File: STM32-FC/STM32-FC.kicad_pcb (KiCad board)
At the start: 4 copper layers, 39 x 48.5 mm, 114 parts, among them J1 GH 1.25mm 6P, J10 GH 1.25mm 6P, J11 GH 1.25mm 6P, J12 GH 1.25mm 6P, J13 GH 1.25mm 4P, J14 GH 1.25mm 4P, J15 GH 1.25mm 4P, J2 USB_C_USB2.0_14P, J3 GH 1.25mm 6P, J4 TF-06A, J5 JST ZH 1.5mm 2P, J6 PWM_Conn_3x14, J7 ZH 1.5mm 3P, J8 ZH 1.5mm 4P, J9 GH 1.25mm 10P, Q1 S9013, Q2 S9013, SW2 SW_DIP_x03, U1 STM32F407VETx, U10 ATA6561-GBQW, U11 ATA6561-GBQW, U2 USBLC6-2SC6, U3 AMS1117-3.3, U4 AMS1117-3.3, U5 W25X40CLUXIG, U6 BMI323, U7 ICM-42688-P, U8 LIS2MDLTR, U9 LPS22HH, Y1 16MHz

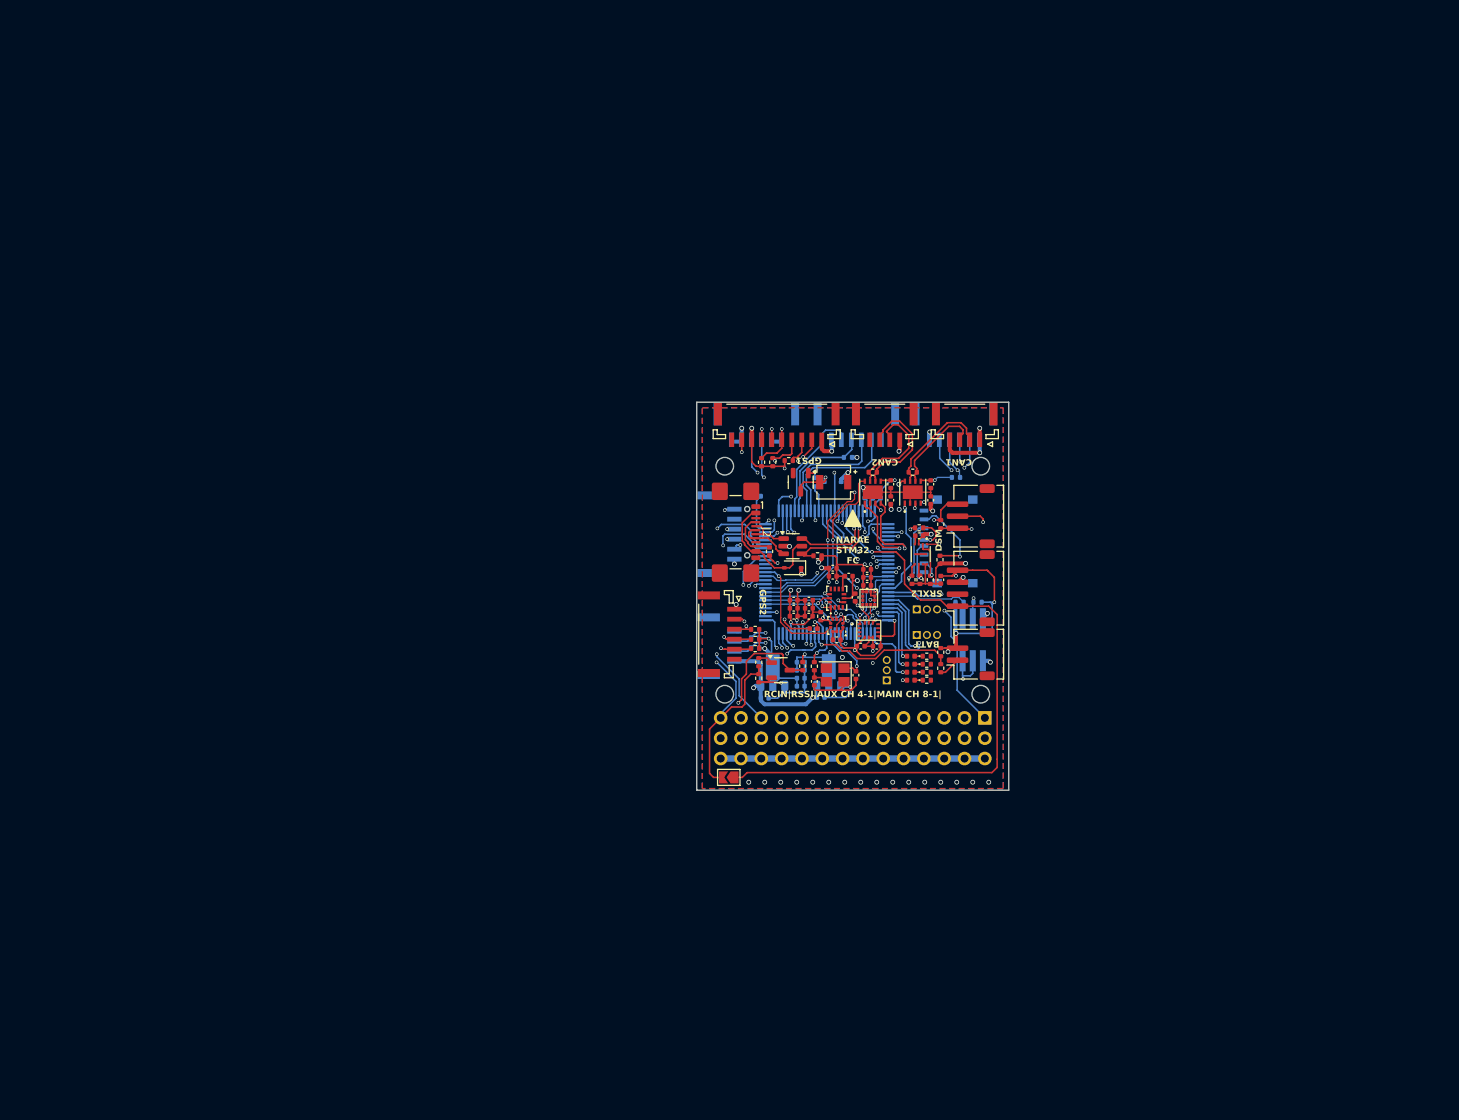
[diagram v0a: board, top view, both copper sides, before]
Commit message: update : BJT to MOSFET
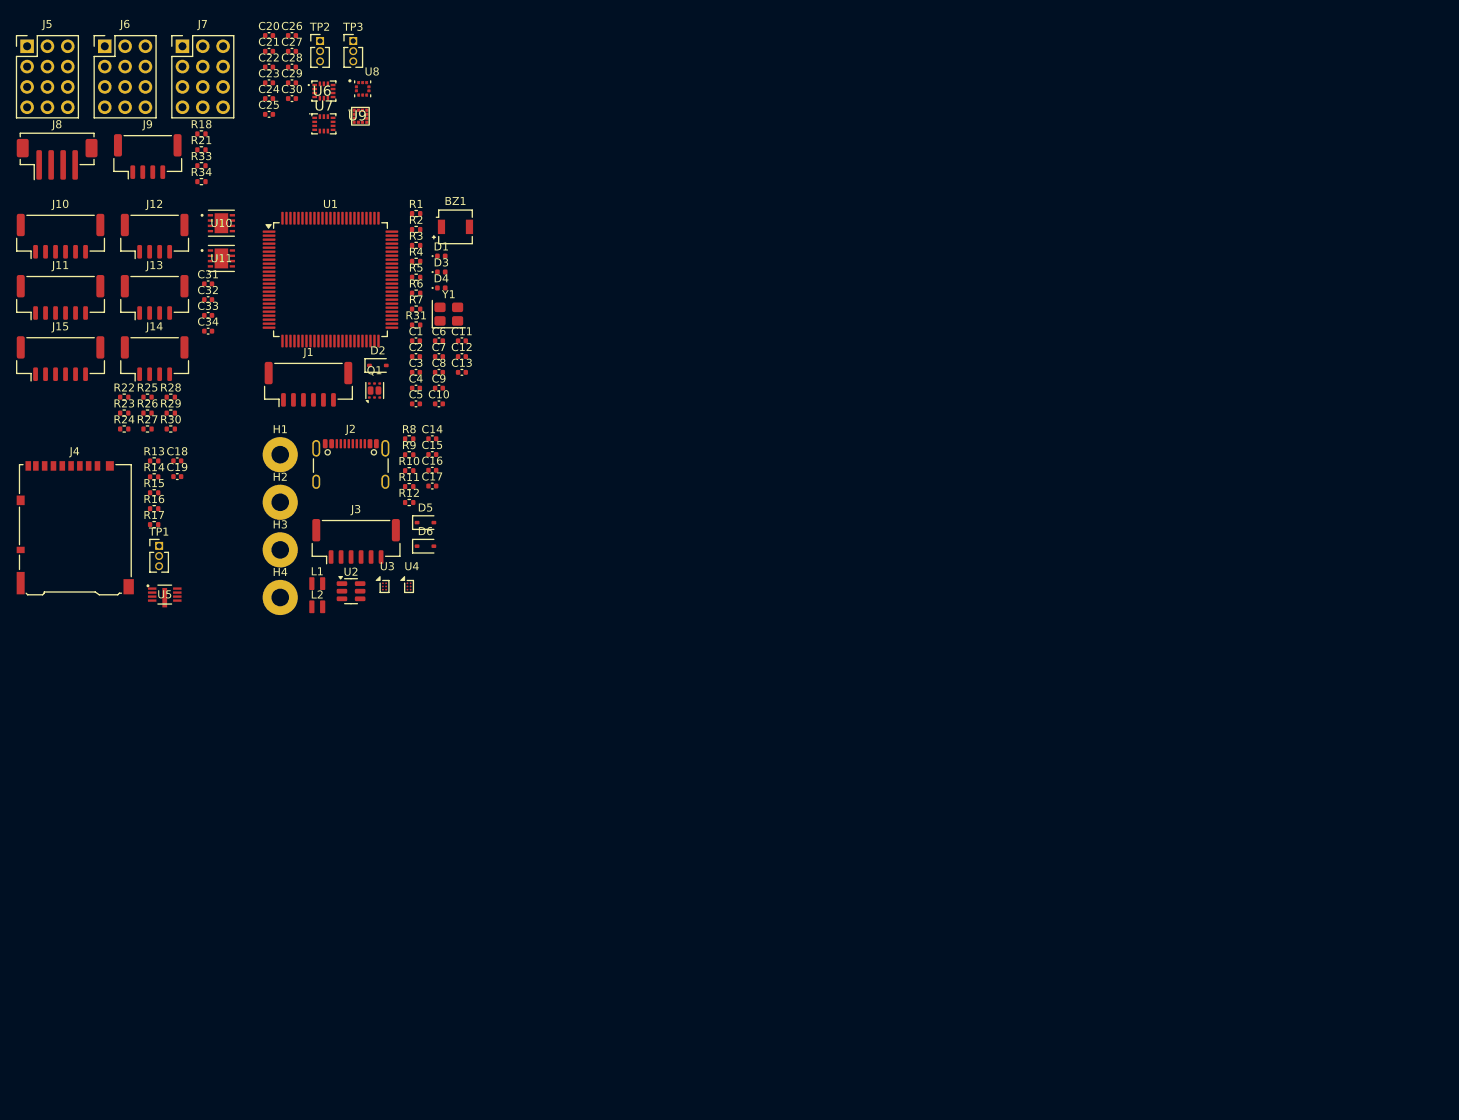
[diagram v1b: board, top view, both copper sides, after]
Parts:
- removed C35: 100nF, Capacitor_SMD:C_0402_1005Metric
- removed JP1: SolderJumper_2_Open, Jumper:SolderJumper-2_P1.3mm_Open_TrianglePad1.0x1.5mm
- removed Q2: S9013, Package_TO_SOT_SMD:SOT-23-3
- removed R19, R20, R32: 10k, Resistor_SMD:R_0402_1005Metric
- removed SW2: SW_DIP_x03, Button_Switch_SMD:SW_DIP_SPSTx03_Slide_KingTek_DSHP03TJ_W5.25mm_P1.27mm_JPin
- added L1: 2.2u, VLS201610ET-2R2M:VLS201610ET-2R2M, F.Cu at (72.1, 92.2)
- added L2: 2.2u, VLS201610ET-2R2M:VLS201610ET-2R2M, F.Cu at (72.1, 95.1)
- C11: value 1uF -> 100nF; moved to F.Cu
- C12: value 100nF -> 1uF; moved to F.Cu
- C13, C18: value 10uF -> 100nF; moved to F.Cu
- C14: value 10uF -> 4.7uF; moved to F.Cu
- C15: value 100nF -> 4.7uF; moved to F.Cu
- C16: value 100nF -> 10uF; moved to F.Cu
- C17, R1, R29, R30, R31, TP1, TP2, TP3, U1: moved to F.Cu
- C20: value 100nF -> 10nF
- C21: value 100nF -> 100pF
- C22: value 100pF -> 100nF
- C23: value 100nF -> 2.2nF
- C24: value 2.2nF -> 100nF
- C25: value 10nF -> 100nF
- C26: value 4.7uF -> 10uF
- C27: value 10uF -> 100nF
- C29: value 100nF -> 220nF
- C30: value 220nF -> 100nF
- C5, C6: value 2.2uF -> 100nF; moved to F.Cu
- C7, C8: value 100nF -> 2.2uF
- D1: value White -> Red
- D2: value Red -> B5819W; footprint LED_SMD:LED_0402_1005Metric -> Diode_SMD:D_SOD-323
- D3: value B5819W -> Yellow; footprint Diode_SMD:D_SOD-323 -> LED_SMD:LED_0402_1005Metric; moved to F.Cu
- D4: value Yellow -> Blue
- D5: value Blue -> B5819W; footprint LED_SMD:LED_0402_1005Metric -> Diode_SMD:D_SOD-323
- H1, H2, H3, H4: footprint Hole:MountingHole_2.2mm_M2 -> MountingHole:MountingHole_2.2mm_M2_Pad
- J1, J11, J3: footprint JST_GH:JST_GH_SM06B-GHS-TB_06x1.25mm_Angled -> Connector_JST:JST_GH_BM06B-GHS-TBT_1x06-1MP_P1.25mm_Vertical; moved to F.Cu
- J10: footprint JST_GH:JST_GH_SM06B-GHS-TB_06x1.25mm_Angled -> Connector_JST:JST_GH_BM06B-GHS-TBT_1x06-1MP_P1.25mm_Vertical
- J12: value GH 1.25mm 6P -> GH 1.25mm 4P; footprint JST_GH:JST_GH_SM06B-GHS-TB_06x1.25mm_Angled -> Connector_JST:JST_GH_BM04B-GHS-TBT_1x04-1MP_P1.25mm_Vertical; moved to F.Cu
- J13: footprint JST_GH:JST_GH_SM04B-GHS-TB_04x1.25mm_Angled -> Connector_JST:JST_GH_BM04B-GHS-TBT_1x04-1MP_P1.25mm_Vertical; moved to F.Cu
- J14: footprint JST_GH:JST_GH_SM04B-GHS-TB_04x1.25mm_Angled -> Connector_JST:JST_GH_BM04B-GHS-TBT_1x04-1MP_P1.25mm_Vertical
- J15: value GH 1.25mm 4P -> GH 1.25mm 6P; footprint JST_GH:JST_GH_SM04B-GHS-TB_04x1.25mm_Angled -> Connector_JST:JST_GH_BM06B-GHS-TBT_1x06-1MP_P1.25mm_Vertical
- J2: value USB_C_USB2.0_14P -> USB_C_USB2.0_16P; footprint Connector_USB:USB_C_Receptacle_GCT_USB4110 -> Connector_USB:USB_C_Receptacle_GCT_USB4105-xx-A_16P_TopMnt_Horizontal
- J4: value TF-06A -> DM3AT-SF-PEJM5; footprint TF-06A:TF06A -> Connector_Card:microSD_HC_Hirose_DM3AT-SF-PEJM5; moved to F.Cu
- J5: value JST ZH 1.5mm 2P -> PWM_Conn_3x04; footprint JST_ZH:JST_ZH_S2B-ZR-SM4A-TF_1x02-1MP_P1.50mm_Horizontal -> PWM_Connector:PWM_Conn_3x04_JLC
- J6: value PWM_Conn_3x14 -> PWM_Conn_3x04; footprint PWM_Connector:PWM_Conn_3x14 -> PWM_Connector:PWM_Conn_3x04_JLC; moved to F.Cu
- J7: value ZH 1.5mm 3P -> PWM_Conn_3x04; footprint JST_ZH:JST_ZH_S3B-ZR-SM4A-TF_1x03-1MP_P1.50mm_Horizontal -> PWM_Connector:PWM_Conn_3x04_JLC
- J8: footprint JST_ZH:JST_ZH_S4B-ZR-SM4A-TF_1x04-1MP_P1.50mm_Horizontal -> Connector_JST:JST_ZH_B4B-ZR-SM4-TF_1x04-1MP_P1.50mm_Vertical
- J9: value GH 1.25mm 10P -> GH 1.25mm 4P; footprint JST_GH:JST_GH_SM10B-GHS-TB_10x1.25mm_Angled -> Connector_JST:JST_GH_BM04B-GHS-TBT_1x04-1MP_P1.25mm_Vertical
- Q1: value S9013 -> PMDPB30XN; footprint Package_TO_SOT_SMD:SOT-23-3 -> Nexperia_PMD:Nexperia_SOT1118
- R11, R12: value 10k -> 267k
- R17: value 15k -> 10k
- R18, R21: value 1k -> 10k
- R2: value 100k -> 4k7; moved to F.Cu
- R26, R27: value 10k -> 120
- R3: value 4k7 -> 100k
- R34: value 120 -> 10k
- R4: value 1k -> 120
- R5: value 180 -> 1k; moved to F.Cu
- R8: value 1k -> 5k1
- U3, U4: value AMS1117-3.3 -> TPS62840YBG; footprint Package_TO_SOT_SMD:SOT-89-3 -> Package_BGA:Texas_DSBGA-6_0.855x1.255mm_Layout2x3_P0.4mm_LevelC; moved to F.Cu
- U5: footprint W25X40CLUX:USON_LUXIG TR_WIN-L -> W25X40CLUX:USON_LUXIG_TR_HandSolder
- U6: value BMI323 -> ICM-42688-P; footprint BMI323:BMI323_L -> ICM-42688-P:IIM42352_L
- U7: value ICM-42688-P -> ICM-45686; footprint ICM-42688-P:IIM42352_L -> ICM-45686:ICM-45686
- U8: value LIS2MDLTR -> ICP-20100; footprint LIS2MDLTR:LIS2MDLTR -> ICP-20100:ICP-20100
- U9: value LPS22HH -> LIS2MDLTR; footprint LPS22HH:ST_HLGA-10_2x2mm_P0.5mm_LayoutBorder3x2y -> LIS2MDLTR:LIS2MDLTR
- moved J5 136.0 mm to (38.3, 29.1), turned to 0 degrees
- moved J8 126.2 mm to (39.5, 39.1), turned to 0 degrees
- moved J6 122.8 mm to (48.0, 29.1), turned to 0 degrees
- moved J15 113.3 mm to (40.0, 64.0), turned to 0 degrees
- moved J11 112.9 mm to (40.0, 56.4)
- moved R18 112.9 mm to (57.6, 36.0), turned to 0 degrees
- moved J7 110.5 mm to (57.8, 29.1), turned to 0 degrees
- moved J4 109.4 mm to (41.8, 85.2), turned to 0 degrees
- moved C20 108.1 mm to (66.0, 23.7), turned to 0 degrees
- moved TP2 106.8 mm to (72.4, 24.4)
- moved C21 104.9 mm to (66.0, 25.6)
- moved C23 103.6 mm to (66.0, 29.6)
- moved TP3 102.3 mm to (76.6, 24.4), turned to 0 degrees
- moved C26 101.7 mm to (68.9, 23.7)
- moved R17 100.0 mm to (51.7, 84.8), turned to 0 degrees
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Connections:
- net /OSC_IN renamed Net-(U1-PH0)
- net /TIM5_CH3 renamed /MAIN7
- C13 pad 1: +5V -> +3.3V
- C15 pad 1: +3.3V -> +5V
- C16 pad 1: +3.3V_RC -> +3.3V
- C17 pad 1: +3.3V -> +3.3VA
- C18 pad 1: +3.3V_RC -> +3.3V
- C20 pad 1: +3.3V -> +3.3VA
- C21 pad 1: +3.3V -> +3.3VA
- C22 pad 1: +3.3V -> +3.3VA
- C23 pad 1: GND -> +3.3VA
- C23 pad 2: +3.3V -> GND
- C24 pad 1: +3.3V -> +3.3VA
- C25 pad 1: +3.3V -> GND
- C25 pad 2: GND -> +3.3VA
- C26 pad 1: GND -> +3.3VA
- C26 pad 2: +3.3V -> GND
- C27 pad 1: +3.3V -> +3.3VA
- C28 pad 1: +3.3V -> +3.3VA
- C29 pad 1: +3.3V -> Net-(U9-C1)
- C30 pad 1: /Sensors/MAG_C1 -> GND
- C30 pad 2: GND -> +3.3VA
- C5 pad 1: GND -> /NRST
- C5 pad 2: /VCAP1 -> GND
- C6 pad 1: /VCAP2 -> +3.3V
- C7 pad 1: +3.3V -> GND
- C7 pad 2: GND -> Net-(U1-VCAP_1)
- C8 pad 1: +3.3V -> Net-(U1-VCAP_2)
- D1 pad 2: +3.3V -> /LED_RED
- D2 pad 1: Net-(D2-K) -> +5V
- D2 pad 2: /LED_RED -> Net-(BZ1-+)
- D3 pad 1: +5V -> Net-(D3-K)
- D3 pad 2: Net-(BZ1-+) -> /LED_YELLOW
- D4 pad 2: /LED_YELLOW -> /LED_BLUE
- D5 pad 1: Net-(D5-K) -> +5V
- D5 pad 2: /LED_BLUE -> +5V_PWM
- J10 pad 2: /UART5_TX -> /UART2_TX
- J10 pad 3: /UART5_RX -> /UART2_RX
- J10 pad 4: /I2C2_SCL -> /UART2_CTS
- J10 pad 5: /I2C2_SDA -> /UART2_RTS
- J11 pad 2: /UART2_TX -> /UART3_TX
- J11 pad 3: /UART2_RX -> /UART3_RX
- J11 pad 4: /UART2_CTS -> /Communication/TELE2_CTS
- J11 pad 5: /UART2_RTS -> /Communication/TELE2_RTS
- J12 pad 2: /UART3_TX -> /I2C1_SCL
- J12 pad 3: /UART3_RX -> /I2C1_SDA
- J12 pad 4: /UART3_CTS -> GND
- J13 pad 2: /I2C1_SCL -> /Communication/CAN1_P
- J13 pad 3: /I2C1_SDA -> /Communication/CAN1_N
- J14 pad 2: /Communication/CAN1_P -> /Communication/CAN2_P
- J14 pad 3: /Communication/CAN1_N -> /Communication/CAN2_N
- J15 pad 2: /Communication/CAN2_P -> /GPS1_TX
- J15 pad 3: /Communication/CAN2_N -> /GPS1_RX
- J15 pad 4: GND -> /GPS1_SCL
- J2 pad A8: (no net) -> unconnected-(J2-SBU1-PadA8)
- J2 pad B5: Net-(J2-CC1) -> Net-(J2-CC2)
- J2 pad B8: (no net) -> unconnected-(J2-SBU2-PadB8)
- J4 pad 1: unconnected-(J4-RSV_1-Pad1) -> /MSD.D2
- J4 pad 2: /MSD_NSS -> /MSD.D3
- J4 pad 3: /SPI2_MOSI -> /MSD_CMD
- J4 pad 5: /SPI2_SCK -> /MSD.CK
- J4 pad 7: /SPI2_MISO -> /MSD.D0
- J4 pad 8: unconnected-(J4-RSV_2-Pad8) -> /MSD.D1
- J5 pad 1: +BATT -> /MAIN1
- J5 pad 2: GND -> +5V_PWM
- J6 pad 1: /TIM4_CH2 -> /MAIN5
- J6 pad 10: /TIM3_CH4 -> /MAIN8
- J6 pad 11: /TIM1_CH2 -> +5V_PWM
- J6 pad 12: /TIM1_CH3 -> GND
- J6 pad 2: /TIM3_CH1 -> +5V_PWM
- J6 pad 3: /TIM3_CH2 -> GND
- J6 pad 4: /TIM4_CH4 -> /MAIN6
- J6 pad 5: /TIM5_CH1 -> +5V_PWM
- J6 pad 6: /TIM5_CH2 -> GND
- J6 pad 8: /TIM5_CH4 -> +5V_PWM
- J6 pad 9: /TIM3_CH3 -> GND
- J7 pad 1: +3.3V_RC -> /RC_RX
- J7 pad 2: GND -> +5V
- J7 pad 3: /UART1_RX -> GND
- J8 pad 1: /UART1_TX -> /RC_TX
- J9 pad 1: +5V -> /RC_TX
- J9 pad 2: /UART4_TX -> /RC_RX
- J9 pad 3: /UART4_RX -> +5V
- J9 pad 4: /I2C3_SCL -> GND
- Q1 pad 1: Net-(Q1-B) -> GND
- Q1 pad 2: GND -> Net-(Q1A-G)
- Q1 pad 3: Net-(BZ1-+) -> /RC_RX
- R11 pad 1: +3.3V -> GND
- R11 pad 2: /SPI2_MISO -> Net-(U3-VSET)
- R12 pad 1: +3.3V -> GND
- R12 pad 2: /SPI2_SCK -> Net-(U4-VSET)
- R13 pad 2: /SPI2_MOSI -> /MSD.D2
- R14 pad 2: /MSD_NSS -> /MSD.D2
- R15 pad 1: /MSD_DETECT -> +3.3V
- R15 pad 2: Net-(J4-SWICTH) -> /MSD_CMD
- R16 pad 2: /BARO_NSS -> /MSD.D0
- R17 pad 1: +BATT -> +3.3V
- R17 pad 2: /V_BATT -> /MSD.D1
- R18 pad 1: /V_BATT -> +3.3V
- R18 pad 2: GND -> /RC_RX
- R2 pad 1: GND -> Net-(C4-Pad1)
- R2 pad 2: /BOOT1 -> Net-(U1-PH1)
- R21 pad 1: /TIM1_CH4 -> +3.3V
- R21 pad 2: Net-(Q2-B) -> /RC_RX
- R22 pad 1: +3.3V_RC -> +3.3V
- R22 pad 2: /UART1_RX -> /UART2_RX
- R23 pad 2: /I2C3_SDA -> /UART3_RX
- R24 pad 2: /I2C3_SCL -> /I2C1_SDA
- R25 pad 2: /I2C2_SDA -> /I2C1_SCL
- R26 pad 1: +3.3V -> /Communication/CAN1_P
- R26 pad 2: /UART4_RX -> /Communication/CAN1_N
- R27 pad 1: +3.3V -> /Communication/CAN2_P
- R27 pad 2: /I2C2_SCL -> /Communication/CAN2_N
- R28 pad 2: /UART5_RX -> /GPS1_SDA
- R29 pad 2: /UART2_RX -> /GPS1_SCL
- R3 pad 1: Net-(C4-Pad1) -> GND
- R3 pad 2: /OSC_OUT -> /BOOT1
- R30 pad 2: /UART3_RX -> /GPS1_RX
- R31 pad 1: +3.3V -> Net-(Q1A-G)
- R31 pad 2: /I2C1_SDA -> GND
- R33 pad 1: /Communication/CAN1_P -> /SERVO & RC/SBUS
- R33 pad 2: /Communication/CAN1_N -> Net-(Q1B-G)
- R34 pad 1: /Communication/CAN2_P -> Net-(Q1B-G)
- R34 pad 2: /Communication/CAN2_N -> GND
- R4 pad 1: Net-(D1-K) -> /Buzzer
- R4 pad 2: GND -> Net-(Q1A-G)
- R5 pad 1: /Buzzer -> Net-(D1-K)
- R5 pad 2: Net-(Q1-B) -> GND
- R6 pad 1: Net-(D2-K) -> Net-(D3-K)
- R8 pad 1: Net-(D5-K) -> Net-(J2-CC1)
- R9 pad 1: Net-(J2-CC1) -> Net-(J2-CC2)
- TP1 pad 1: /SPI2_SCK -> /MEM_SCK
- TP1 pad 2: /SPI2_MISO -> /MEM_MOSI
- TP1 pad 3: /SPI2_MOSI -> /MEM_MISO
- TP2 pad 1: /SPI1_SCK -> /SEN1_SCK
- TP2 pad 2: /SPI1_MISO -> /SEN1_MOSI
- TP2 pad 3: /SPI1_MOSI -> /SEN1_MISO
- TP3 pad 1: /SPI3_SCK -> /SEN2_SCK
- TP3 pad 2: /SPI3_MISO -> /SEN2_MOSI
- TP3 pad 3: /SPI3_MOSI -> /SEN2_MISO
- U1 pad 13: /OSC_OUT -> Net-(U1-PH1)
- U1 pad 15: /V_BATT -> unconnected-(U1-PC0-Pad15)
- U1 pad 16: /RSSI_IN -> unconnected-(U1-PC1-Pad16)
- U1 pad 2: /GYRO2_NSS -> unconnected-(U1-PE3-Pad2)
- U1 pad 23: /TIM5_CH1 -> /MAIN5
- U1 pad 24: /TIM5_CH2 -> /MAIN6
- U1 pad 26: /TIM5_CH4 -> /MAIN8
- U1 pad 3: /MAG_NSS -> unconnected-(U1-PE4-Pad3)
- U1 pad 30: /SPI1_SCK -> /SEN1_SCK
- U1 pad 31: /SPI1_MISO -> /SEN1_MISO
- U1 pad 32: /SPI1_MOSI -> /SEN1_MOSI
- U1 pad 35: /TIM3_CH3 -> unconnected-(U1-PB0-Pad35)
- U1 pad 36: /TIM3_CH4 -> unconnected-(U1-PB1-Pad36)
- U1 pad 38: /BARO_INT -> /GYRO1_NSS
- U1 pad 39: unconnected-(U1-PE8-Pad39) -> /GYRO2_NSS
- U1 pad 4: /GYRO1_NSS -> /Buzzer
- U1 pad 40: unconnected-(U1-PE9-Pad40) -> /MAG_NSS
- U1 pad 41: unconnected-(U1-PE10-Pad41) -> /BARO_NSS
- U1 pad 42: /TIM1_CH2 -> /FLASH_NSS
- U1 pad 44: /TIM1_CH3 -> unconnected-(U1-PE13-Pad44)
- U1 pad 45: /TIM1_CH4 -> /PPM_IN
- U1 pad 47: /I2C2_SCL -> /GPS1_SCL
- U1 pad 48: /I2C2_SDA -> /GPS1_SDA
- U1 pad 49: /VCAP1 -> Net-(U1-VCAP_1)
- U1 pad 5: /BARO_NSS -> unconnected-(U1-PE6-Pad5)
- U1 pad 52: /SPI2_SCK -> /MEM_SCK
- U1 pad 53: /SPI2_MISO -> /MEM_MISO
- U1 pad 54: /SPI2_MOSI -> /MEM_MOSI
- U1 pad 57: /GPS1_SW_LED -> unconnected-(U1-PD10-Pad57)
- U1 pad 58: /UART3_CTS -> unconnected-(U1-PD11-Pad58)
- U1 pad 59: /UART3_RTS -> /MAIN1
- U1 pad 60: /GPS1_SW -> /MAIN2
- U1 pad 61: /Buzzer -> /MAIN3
- U1 pad 62: /TIM4_CH4 -> /MAIN4
- U1 pad 63: /TIM3_CH1 -> /GPS1_TX
- U1 pad 64: /TIM3_CH2 -> /GPS1_RX
- U1 pad 65: /GPS1_BUZZER -> /MSD.D0
- U1 pad 66: /I2C3_SDA -> /MSD.D1
- U1 pad 67: /I2C3_SCL -> unconnected-(U1-PA8-Pad67)
- U1 pad 68: /UART1_TX -> /RC_TX
- U1 pad 69: /UART1_RX -> /RC_RX
- U1 pad 7: /FLASH_NSS -> unconnected-(U1-PC13-Pad7)
- U1 pad 73: /VCAP2 -> Net-(U1-VCAP_2)
- U1 pad 78: /UART4_TX -> /MSD.D2
- U1 pad 79: /UART4_RX -> /MSD.D3
- U1 pad 80: /UART5_TX -> /MSD.CK
- U1 pad 83: /UART5_RX -> /MSD_CMD
- U1 pad 88: /MSD_NSS -> unconnected-(U1-PD7-Pad88)
- U1 pad 89: /SPI3_SCK -> /SEN2_SCK
- U1 pad 90: /SPI3_MISO -> /SEN2_MISO
- U1 pad 91: /SPI3_MOSI -> /SEN2_MOSI
- U1 pad 93: /TIM4_CH2 -> unconnected-(U1-PB7-Pad93)
- U2 pad 1: /USB & POWER/USB_CONN_D- -> /USB_D-
- U2 pad 3: /USB & POWER/USB_CONN_D+ -> /USB & POWER/USB_CONN_D-
- U2 pad 4: /USB_D+ -> /USB & POWER/USB_CONN_D+
- U2 pad 6: /USB_D- -> /USB_D+
- U5 pad 2: /SPI2_MISO -> /MEM_MISO
- U5 pad 5: /SPI2_MOSI -> /MEM_MOSI
- U5 pad 6: /SPI2_SCK -> /MEM_SCK
- U6 pad 1: /SPI3_MISO -> /SEN1_MISO
- U6 pad 12: /GYRO2_NSS -> /GYRO1_NSS
- U6 pad 13: /SPI3_SCK -> /SEN1_SCK
- U6 pad 14: /SPI3_MOSI -> /SEN1_MOSI
- U6 pad 5: +3.3V -> +3.3VA
- U6 pad 7: GND -> unconnected-(U6-RESV_7-Pad7)
- U6 pad 8: +3.3V -> +3.3VA
- U7 pad 1: /SPI1_MISO -> /SEN2_MISO
- U7 pad 12: /GYRO1_NSS -> /GYRO2_NSS
- U7 pad 13: /SPI1_SCK -> /SEN2_SCK
- U7 pad 14: /SPI1_MOSI -> /SEN2_MOSI
- U7 pad 5: +3.3V -> +3.3VA
- U7 pad 8: +3.3V -> +3.3VA
- U8 pad 1: /SPI3_SCK -> /BARO_NSS
- U8 pad 10: +3.3V -> +3.3VA
- U8 pad 2: unconnected-(U8-NC1-Pad2) -> /SEN1_SCK
- U8 pad 3: /MAG_NSS -> GND
- U8 pad 4: /SPI3_MOSI -> /SEN1_MOSI
- U8 pad 5: /Sensors/MAG_C1 -> +3.3VA
- U8 pad 6: GND -> /SEN1_MISO
- U8 pad 7: /SPI3_MISO -> unconnected-(U8-INT-Pad7)
- U8 pad 9: +3.3V -> GND
- U9 pad 1: +3.3V -> /SEN1_SCK
- U9 pad 10: +3.3V -> +3.3VA
- U9 pad 2: /SPI1_SCK -> unconnected-(U9-NC1-Pad2)
- U9 pad 3: GND -> /MAG_NSS
- U9 pad 4: /SPI1_MOSI -> /SEN1_MOSI
- U9 pad 5: /SPI1_MISO -> Net-(U9-C1)
- U9 pad 6: /BARO_NSS -> GND
- U9 pad 7: /BARO_INT -> /SEN1_MISO
- U9 pad 9: GND -> +3.3VA
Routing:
- net GND: track 169.1 -> 0.00 mm, vias 41 -> 0
- net +3.3V: track 130.5 -> 0.00 mm, vias 24 -> 0
- net /UART1_RX: track 119.1 -> 0.00 mm, vias 3 -> 0
- net /UART1_TX: track 79.7 -> 0.00 mm, vias 1 -> 0
- net /UART5_TX: track 62.3 -> 0.00 mm, vias 2 -> 0
- net /UART5_RX: track 56.6 -> 0.00 mm, vias 2 -> 0
- net +3.3V_RC: track 54.9 -> 0.00 mm, vias 3 -> 0
- net +5V: track 53.2 -> 0.00 mm, vias 16 -> 0
- net /TIM1_CH4: track 52.9 -> 0.00 mm, vias 2 -> 0
- net +5V_PWM: track 40.1 -> 0.00 mm, vias 1 -> 0
- net /TIM3_CH1: track 39.3 -> 0.00 mm, vias 1 -> 0
- net /SPI2_MOSI: track 38.8 -> 0.00 mm, vias 2 -> 0
- net /TIM3_CH2: track 37.5 -> 0.00 mm, vias 1 -> 0
- net /TIM4_CH4: track 36.6 -> 0.00 mm, vias 1 -> 0
- net /BOOT1: track 35.5 -> 0.00 mm, vias 2 -> 0
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- removed copper zone on In2.Cu, net +3.3V
- removed copper zone on In1.Cu, net +5V
- removed copper zone on B.Cu, net GND
- removed copper zone on F.Cu, net GND
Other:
- board outline removed
- board text removed: "BATT"
- board text removed: "CAN1"
- board text removed: "CAN2"
- board text removed: "DEBUG"
- board text removed: "DSM"
- board text removed: "GPS1"
- board text removed: "GPS2"
- board text removed: "I2C"
- board text removed: "NARAE STM32 FC"
- board text removed: "POWER"
- board text removed: "RCIN|RSSI|AUX CH 4-1|MAIN CH 8-1|"
- board text removed: "SPI1"
- board text removed: "SPI2"
- board text removed: "SPI3"
- board text removed: "SRXL2"
- board text removed: "TELEM1"
- board text removed: "TELEM2"

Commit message: WIP : pcb part layout &* BOM udpate
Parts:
- U5: footprint W25X40CLUX:USON_LUXIG_TR_HandSolder -> W25X40CLUX:USON_LUXIG TR_WIN
- U8: value ICP-20100 -> PQFN50P200X200X85-10N
- U9: value LIS2MDLTR -> LGA-12
- moved J5 164.8 mm to (168.7, 130.0), turned to -90 degrees
- moved J6 147.8 mm to (156.0, 130.0), turned to -90 degrees
- moved TP2 143.1 mm to (188.0, 108.7)
- moved TP3 143.1 mm to (192.2, 108.7)
- moved J4 125.7 mm to (167.0, 74.0), turned to 180 degrees
- moved C20 122.8 mm to (149.0, 114.3), turned to 90 degrees
- moved C24 121.2 mm to (152.5, 116.5)
- moved C22 121.0 mm to (151.0, 113.8), turned to -90 degrees
- moved C21 118.4 mm to (147.5, 111.5), turned to 180 degrees
- moved J7 114.9 mm to (130.0, 118.5), turned to 180 degrees
- moved C23 114.8 mm to (147.5, 110.5), turned to 180 degrees
- moved U9 114.6 mm to (153.0, 120.0), turned to 180 degrees
- moved U8 113.3 mm to (147.0, 120.0)
- moved U7 112.7 mm to (153.0, 114.0), turned to -90 degrees
- moved U6 111.6 mm to (147.0, 114.0), turned to 90 degrees
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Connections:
- U1 pad 52: /MEM_SCK -> /SEN2_SCK
- U1 pad 53: /MEM_MISO -> /SEN2_MISO
- U1 pad 54: /MEM_MOSI -> /SEN2_MOSI
- U1 pad 89: /SEN2_SCK -> /MEM_SCK
- U1 pad 90: /SEN2_MISO -> /MEM_MISO
- U1 pad 91: /SEN2_MOSI -> /MEM_MOSI
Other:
- board outline added: 50 x 70 mm

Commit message: update : AHRS PCB layout & routing done
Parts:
- U8: value PQFN50P200X200X85-10N -> ICP-20100
- U9: value LGA-12 -> LIS2MDLRT
- moved R21 182.1 mm to (201.5, 149.5)
- moved R33 182.1 mm to (201.5, 151.5)
- moved R34 182.1 mm to (201.5, 153.5)
- moved R18 174.7 mm to (203.5, 132.0)
- moved R31 160.2 mm to (212.0, 156.8)
- moved R4 160.2 mm to (212.0, 148.8)
- moved C19 131.3 mm to (185.8, 75.0)
- moved R13 128.0 mm to (179.5, 70.8)
- moved R14 128.0 mm to (179.5, 72.8)
- moved R15 128.0 mm to (179.5, 74.8)
- moved R16 128.0 mm to (179.5, 76.7)
- moved R17 128.0 mm to (179.5, 78.7)
- moved C26 126.1 mm to (150.2, 120.0), turned to 90 degrees
- moved C28 125.9 mm to (152.5, 121.8)
- moved C27 125.2 mm to (151.2, 120.0), turned to 90 degrees
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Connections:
- U9 pad 1: /SEN1_SCK -> /SEN2_SCK
- U9 pad 4: /SEN1_MOSI -> /SEN2_MOSI
- U9 pad 7: /SEN1_MISO -> /SEN2_MISO
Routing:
- net +5V: track 0.00 -> 73.3 mm, vias 0 -> 4
- net +3.3VA: track 0.00 -> 59.7 mm, vias 0 -> 8
- net /SEN2_MISO: track 0.00 -> 24.6 mm, vias 0 -> 4
- net /SEN1_MISO: track 0.00 -> 23.4 mm, vias 0 -> 4
- net /SEN2_MOSI: track 0.00 -> 22.8 mm, vias 0 -> 4
- net +5V_PWM: track 0.00 -> 22.8 mm
- net /SEN2_SCK: track 0.00 -> 22.6 mm, vias 0 -> 1
- net /SEN1_MOSI: track 0.00 -> 22.6 mm, vias 0 -> 3
- net /SEN1_SCK: track 0.00 -> 19.8 mm, vias 0 -> 4
- net VBUS: track 0.00 -> 15.9 mm, vias 0 -> 2
- net GND: track 0.00 -> 13.7 mm, vias 0 -> 12
- net /USB_D-: track 0.00 -> 8.90 mm
- net /USB_D+: track 0.00 -> 8.90 mm
- net Net-(J2-CC2): track 0.00 -> 8.40 mm
- net +3.3V: track 0.00 -> 5.65 mm, vias 0 -> 1
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- added copper zone on F.Cu, net +5V
- added copper zone on F.Cu, net GND
- added copper zone on In1.Cu, net GND
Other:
- board text added: "CAN1"
- board text added: "CAN2"
- board text added: "DEBUG"
- board text added: "ELRS"
- board text added: "GPS"
- board text added: "I2C"
- board text added: "POWER"
- board text added: "SRXL2"
- board text added: "TELE1"
- board text added: "TELE2"

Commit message: PCB layout done
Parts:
- added JP1: SolderJumper_2_Bridged, Jumper:SolderJumper-2_P1.3mm_Bridged_RoundedPad1.0x1.5mm, F.Cu at (142.5, 120.8)
- added R19: 10k, Resistor_SMD:R_0402_1005Metric, F.Cu at (140.2, 97.2)
- moved C3 80.3 mm to (159.5, 94.2), turned to -90 degrees
- moved C2 68.6 mm to (140.5, 103.2), turned to -90 degrees
- moved C12 64.1 mm to (139.2, 105.0), turned to 180 degrees
- moved C6 64.0 mm to (140.8, 98.8), turned to 90 degrees
- moved C13 63.5 mm to (139.2, 106.0), turned to 180 degrees
- moved C9 63.1 mm to (144.2, 90.8)
- moved R31 59.6 mm to (166.5, 118.2)
- moved R4 55.4 mm to (166.5, 117.2), turned to 180 degrees
- moved R34 53.6 mm to (162.0, 117.2), turned to 180 degrees
- moved R33 51.6 mm to (162.0, 118.2)
- moved R21 50.1 mm to (164.8, 115.5), turned to 180 degrees
- moved R18 41.9 mm to (166.3, 112.8)
- moved C19 24.7 mm to (162.8, 84.0), turned to 90 degrees
- moved R13 20.6 mm to (163.8, 84.0), turned to 90 degrees
- moved C18 19.5 mm to (132.8, 88.5), turned to 180 degrees
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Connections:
- C20 pad 2: GND -> GNDA
- C21 pad 2: GND -> GNDA
- C22 pad 2: GND -> GNDA
- C23 pad 2: GND -> GNDA
- C24 pad 2: GND -> GNDA
- C25 pad 1: GND -> GNDA
- C26 pad 2: GND -> GNDA
- C27 pad 2: GND -> GNDA
- C28 pad 2: GND -> GNDA
- C29 pad 2: GND -> GNDA
- C30 pad 1: GND -> GNDA
- R14 pad 2: /MSD.D2 -> /MSD.D3
- U1 pad 1: /LED_BLUE -> /LED_YELLOW
- U1 pad 17: /PM_CURRENT -> /PM_VOLTAGE
- U1 pad 18: /PM_VOLTAGE -> /PM_CURRENT
- U1 pad 2: unconnected-(U1-PE3-Pad2) -> /LED_BLUE
- U1 pad 35: unconnected-(U1-PB0-Pad35) -> /GYRO1_NSS
- U1 pad 36: unconnected-(U1-PB1-Pad36) -> /BARO_NSS
- U1 pad 38: /GYRO1_NSS -> unconnected-(U1-PE7-Pad38)
- U1 pad 39: /GYRO2_NSS -> unconnected-(U1-PE8-Pad39)
- U1 pad 40: /MAG_NSS -> unconnected-(U1-PE9-Pad40)
- U1 pad 41: /BARO_NSS -> unconnected-(U1-PE10-Pad41)
- U1 pad 42: /FLASH_NSS -> /MAG_NSS
- U1 pad 43: unconnected-(U1-PE12-Pad43) -> /GYRO2_NSS
- U1 pad 47: /GPS1_SCL -> /I2C1_SCL
- U1 pad 48: /GPS1_SDA -> /I2C1_SDA
- U1 pad 95: /I2C1_SCL -> /GPS1_SCL
- U1 pad 96: /I2C1_SDA -> /GPS1_SDA
- U1 pad 98: /LED_YELLOW -> /FLASH_NSS
- U6 pad 6: GND -> GNDA
- U7 pad 6: GND -> GNDA
- U8 pad 3: GND -> GNDA
- U8 pad 8: GND -> GNDA
- U8 pad 9: GND -> GNDA
- U9 pad 6: GND -> GNDA
- U9 pad 8: GND -> GNDA
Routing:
- net +5V: track 73.3 -> 223.2 mm, vias 4 -> 15
- net /I2C1_SCL: track 0.00 -> 53.1 mm, vias 0 -> 2
- net /UART3_TX: track 0.00 -> 51.7 mm, vias 0 -> 2
- net /RC_RX: track 0.00 -> 49.6 mm, vias 0 -> 2
- net /UART3_RX: track 0.00 -> 49.4 mm, vias 0 -> 2
- net /MSD_DETECT: track 0.00 -> 48.8 mm, vias 0 -> 2
- net /UART2_TX: track 0.00 -> 47.5 mm
- net /I2C1_SDA: track 0.00 -> 47.2 mm, vias 0 -> 2
- net +3.3V: track 5.65 -> 50.8 mm, vias 1 -> 23
- net /GPS1_TX: track 0.00 -> 44.3 mm, vias 0 -> 2
- net /GPS1_RX: track 0.00 -> 44.1 mm, vias 0 -> 2
- net /CAN2_STBY: track 0.00 -> 41.6 mm, vias 0 -> 3
- net /RC_TX: track 0.00 -> 40.4 mm, vias 0 -> 2
- net /PM_CURRENT: track 0.00 -> 39.8 mm, vias 0 -> 2
- net /PM_VOLTAGE: track 0.00 -> 39.7 mm, vias 0 -> 2
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- added copper zone on In2.Cu, net +3.3V
- added copper zone on B.Cu, net GND
- added copper zone on F.Cu, net GNDA
- added copper zone on In1.Cu, net GNDA
- added copper zone on In2.Cu, net GNDA
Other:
- board text added: "+"
- board text added: "GND"
- board text added: "NARAEON"
- board text added: "PPM/SBUS/TX/RX"
- board text added: "SERVO OUTPUT : 8 - 1"
- board text added: "SPI1"
- board text added: "SPI2"
- board text added: "SPI3"
- board text added: "STM32-based Flight controller NARAE, INHA University, Korea. github.com/NARAE-INHA-UNIV 2025.10.11"
- board text added: "v1.1"
- board text added: "~"
